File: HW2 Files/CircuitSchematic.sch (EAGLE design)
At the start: 23 parts

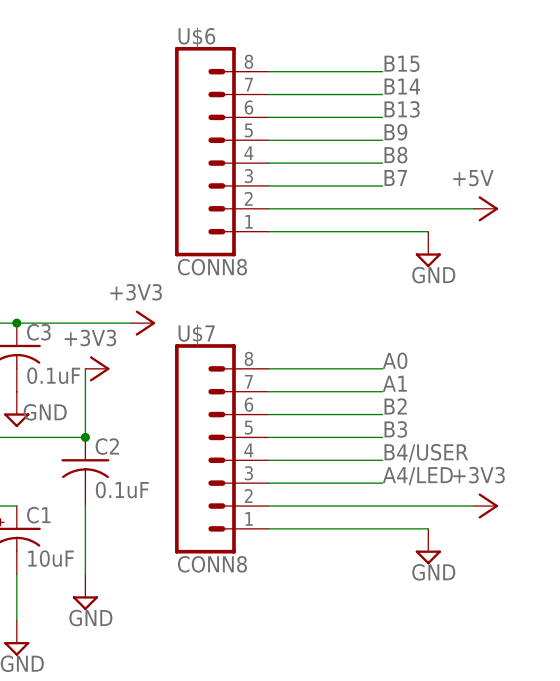
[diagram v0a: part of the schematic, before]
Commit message: Completed PCB
To Do:
- Add silkscreen pin names
- Error checking
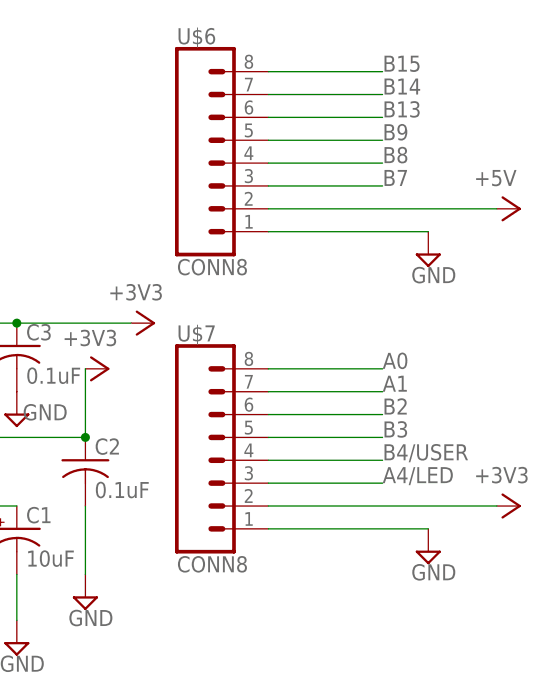
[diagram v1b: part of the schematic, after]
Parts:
- C1, C7: device resistor:CPOL-USB45181A -> resistor:CPOL-USE5-5
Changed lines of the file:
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@@
 <part name="8MHZ-CRYSTAL" library="SparkFun-Connectors" deviceset="CONN_03" device=""/>
 <part name="R1" library="resistor" deviceset="R-US_" device="0207/10" value="10K"/>
-<part name="C1" library="resistor" deviceset="CPOL-US" device="B45181A" value="10uF"/>
+<part name="C1" library="resistor" deviceset="CPOL-US" device="E5-5" value="10uF"/>
 <part name="SUPPLY1" library="supply2" deviceset="GND" device=""/>
 <part name="C2" library="resistor" deviceset="C-US" device="025-025X050" value="0.1uF"/>
@@
 <part name="C5" library="resistor" deviceset="C-US" device="025-025X050" value="0.1uF"/>
 <part name="C6" library="resistor" deviceset="C-US" device="025-025X050" value="0.1uF"/>
-<part name="C7" library="resistor" deviceset="CPOL-US" device="B45181A" value="10uF"/>
+<part name="C7" library="resistor" deviceset="CPOL-US" device="E5-5" value="10uF"/>
 <part name="+3V1" library="supply1" deviceset="+3V3" device=""/>
 <part name="SUPPLY2" library="supply2" deviceset="GND" device=""/>
@@
 <instance part="U$6" gate="G$1" x="152.4" y="78.74"/>
 <instance part="U$7" gate="G$1" x="152.4" y="45.72"/>
-<instance part="+3V6" gate="G$1" x="182.88" y="40.64" rot="R270"/>
-<instance part="P+2" gate="1" x="182.88" y="73.66" rot="R270"/>
+<instance part="+3V6" gate="G$1" x="185.42" y="40.64" rot="R270"/>
+<instance part="P+2" gate="1" x="185.42" y="73.66" rot="R270"/>
 <instance part="SUPPLY12" gate="GND" x="175.26" y="68.58"/>
 <instance part="SUPPLY13" gate="GND" x="175.26" y="35.56"/>
@@
 <pinref part="U$6" gate="G$1" pin="2"/>
 <pinref part="P+2" gate="1" pin="+5V"/>
-<wire x1="157.48" y1="73.66" x2="180.34" y2="73.66" width="0.1524" layer="91"/>
+<wire x1="157.48" y1="73.66" x2="182.88" y2="73.66" width="0.1524" layer="91"/>
 </segment>
 <segment>
@@
 <pinref part="U$7" gate="G$1" pin="2"/>
 <pinref part="+3V6" gate="G$1" pin="+3V3"/>
-<wire x1="157.48" y1="40.64" x2="180.34" y2="40.64" width="0.1524" layer="91"/>
+<wire x1="157.48" y1="40.64" x2="182.88" y2="40.64" width="0.1524" layer="91"/>
 </segment>
 <segment>
@@
 </segment>
 <segment>
+<pinref part="U$5" gate="G$1" pin="1.MCLR"/>
+<wire x1="0" y1="60.96" x2="-10.16" y2="60.96" width="0.1524" layer="91"/>
+<label x="-10.16" y="60.96" size="1.778" layer="95"/>
+</segment>
+<segment>
 <pinref part="U$2" gate="G$1" pin="1"/>
 <wire x1="30.48" y1="114.3" x2="38.1" y2="114.3" width="0.1524" layer="91"/>
@@
 <label x="30.48" y="114.3" size="1.778" layer="95"/>
 </segment>
-<segment>
-<pinref part="U$5" gate="G$1" pin="1.MCLR"/>
-<wire x1="0" y1="60.96" x2="-10.16" y2="60.96" width="0.1524" layer="91"/>
-<label x="-10.16" y="60.96" size="1.778" layer="95"/>
-</segment>
 </net>
 <net name="PGEC1" class="0">
@@
 <pinref part="RED" gate="G$1" pin="C"/>
 <wire x1="96.52" y1="81.28" x2="96.52" y2="83.82" width="0.1524" layer="91"/>
-</segment>
-</net>
-<net name="N$3" class="0">
-<segment>
-<pinref part="GREEN" gate="G$1" pin="C"/>
-<pinref part="R3" gate="G$1" pin="2"/>
-<wire x1="109.22" y1="83.82" x2="109.22" y2="81.28" width="0.1524" layer="91"/>
 </segment>
 </net>
@@
 </segment>
 </net>
+<net name="N$3" class="0">
+<segment>
+<pinref part="GREEN" gate="G$1" pin="C"/>
+<pinref part="R3" gate="G$1" pin="2"/>
+<wire x1="109.22" y1="83.82" x2="109.22" y2="81.28" width="0.1524" layer="91"/>
+</segment>
+</net>
